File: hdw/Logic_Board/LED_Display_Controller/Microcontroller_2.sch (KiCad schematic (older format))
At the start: 1 part, among them U601 PIC32MZ2048EFH144_IPL

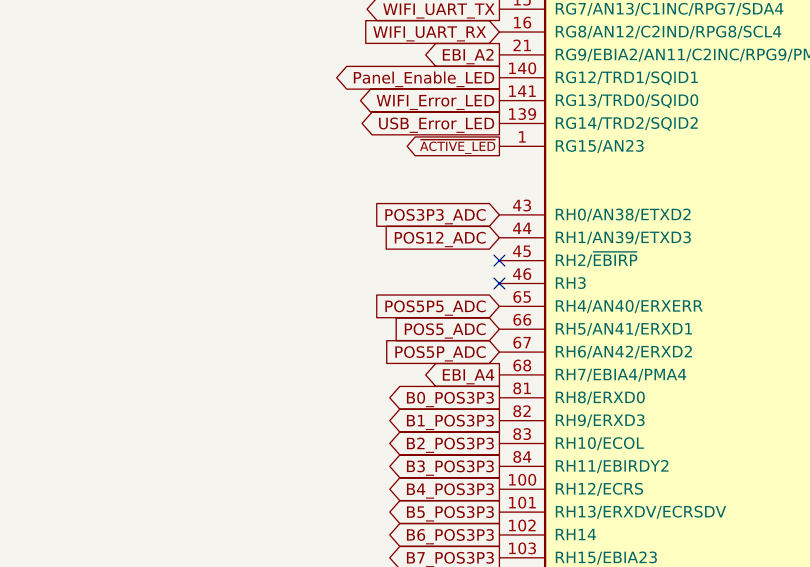
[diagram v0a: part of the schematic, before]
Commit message: Added other error LED
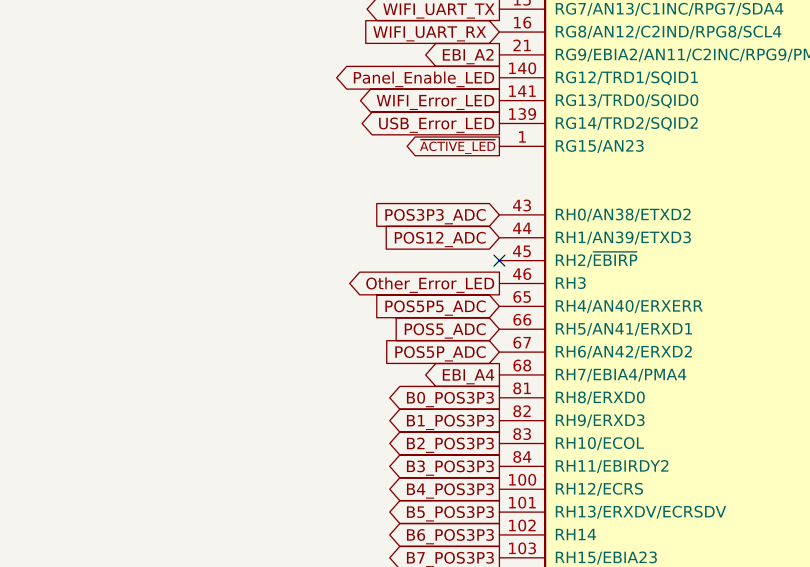
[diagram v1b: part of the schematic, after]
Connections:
- net Other_Error_LED: now reaches U601.46 (RH3)
- no-connect marks 4 -> 3
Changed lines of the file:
@@
 NoConn ~ 4030 1680
 NoConn ~ 4030 4080
-NoConn ~ 4030 4180
 NoConn ~ 7130 1880
 Text Notes 550  700  0    100  ~ 20
@@
 	1    0    0    -1
 $EndComp
+Text GLabel 4030 4180 0    50   Output ~ 0
+Other_Error_LED
 $EndSCHEMATC

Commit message: Added some digikey partnumbers to components
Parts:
- U601: Config ALL -> (none)
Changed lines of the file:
@@
 F 2 "Housings_QFP:TQFP-144_20x20mm_Pitch0.5mm" H 5580 3530 50  0001 C CNN
 F 3 "http://ww1.microchip.com/downloads/en/DeviceDoc/60001320D.pdf" H 5580 3530 50  0001 C CNN
-F 4 "ALL" H 5580 3530 50  0001 C CNN "Config"
+F 4 "" H 5580 3530 50  0001 C CNN "Config"
 F 5 "PIC32MZ2048EFH144-I/PL-ND" H 5580 3530 50  0001 C CNN "Digi-Key PN"
 	3    5580 3530

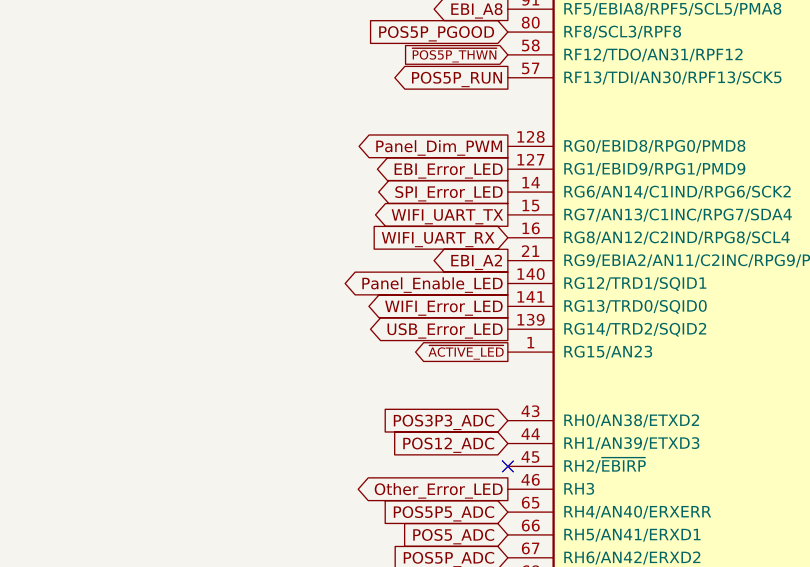
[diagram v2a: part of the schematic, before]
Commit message: Placed decoupling caps around micro
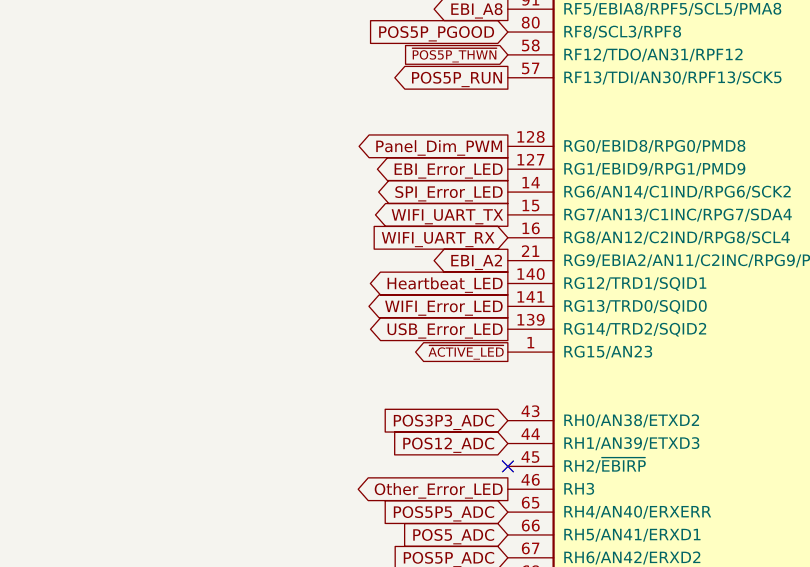
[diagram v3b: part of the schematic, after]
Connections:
- net Panel_Enable_LED renamed Heartbeat_LED
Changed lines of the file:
@@
 USB_Error_LED
 Text GLabel 4030 3280 0    50   Output ~ 0
-Panel_Enable_LED
+Heartbeat_LED
 Text GLabel 4030 2180 0    50   Input ~ 0
 POS5P_PGOOD

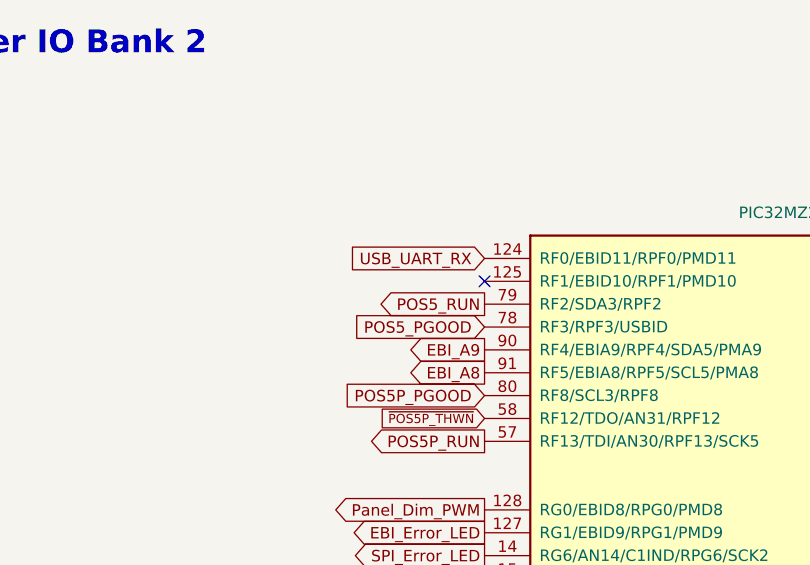
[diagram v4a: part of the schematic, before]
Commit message: More routing, added POS12 PGOOD net to micro
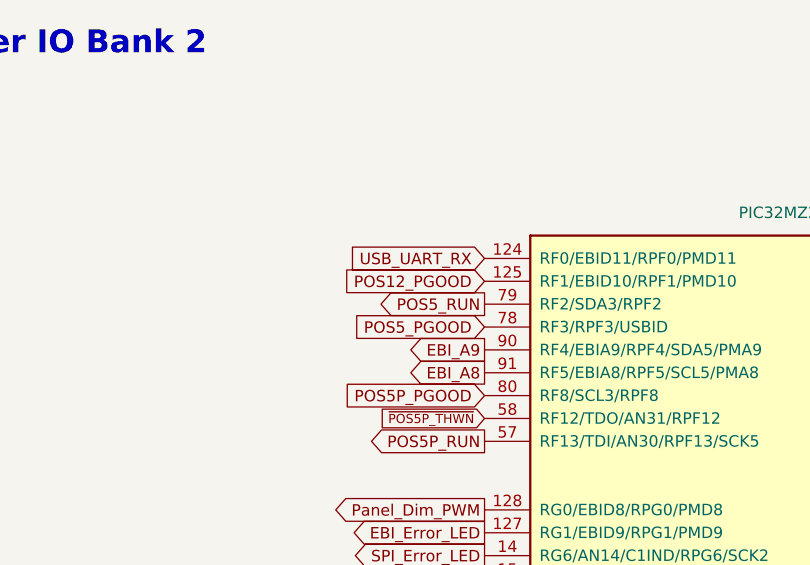
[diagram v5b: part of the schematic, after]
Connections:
- net POS12_PGOOD: now reaches U601.125 (RF1/EBID10/RPF1/PMD10)
- no-connect marks 3 -> 2
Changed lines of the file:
@@
 	1    0    0    -1
 $EndComp
-NoConn ~ 4030 1680
 NoConn ~ 4030 4080
 NoConn ~ 7130 1880
@@
 Text GLabel 4030 4180 0    50   Output ~ 0
 Other_Error_LED
+Text GLabel 4030 1680 0    50   Input ~ 0
+POS12_PGOOD
 $EndSCHEMATC
